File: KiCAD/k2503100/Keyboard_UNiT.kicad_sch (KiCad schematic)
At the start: 71 parts, among them J1 Power, J2 PWM, J3 Analog, J4 PWM, J5 Analog, J6 Communication, J7 Digital, SW1 SW_SPDT, SW10 SW_SPDT, SW11 SW_SPDT, SW12 SW_SPDT, SW13 SW_SPDT, SW14 SW_SPDT, SW15 SW_SPDT, SW16 SW_SPDT, SW17 SW_SPDT, SW18 SW_SPDT, SW19 SW_SPDT, SW2 SW_SPDT, SW20 SW_SPDT, SW21 SW_SPDT, SW22 SW_SPDT, SW23 SW_SPDT, SW24 SW_SPDT, SW25 SW_SPDT, SW26 SW_SPDT, SW27 SW_SPDT, SW28 SW_SPDT, SW29 SW_SPDT, SW3 SW_SPDT, SW30 SW_SPDT, SW31 SW_SPDT, SW32 SW_SPDT, SW33 SW_SPDT, SW34 SW_SPDT, SW35 SW_SPDT, SW36 SW_SPDT, SW37 SW_SPDT, SW38 SW_SPDT, SW39 SW_SPDT, SW4 SW_SPDT, SW40 SW_SPDT, SW41 SW_SPDT, SW42 SW_SPDT, SW43 SW_SPDT, SW44 SW_SPDT, SW45 SW_SPDT, SW46 SW_SPDT, SW47 SW_SPDT, SW48 SW_SPDT, SW49 SW_SPDT, SW5 SW_SPDT, SW50 SW_SPDT, SW51 SW_SPDT, SW52 SW_SPDT, SW53 SW_SPDT, SW54 SW_SPDT, SW55 SW_SPDT, SW56 SW_SPDT, SW57 SW_SPDT, SW58 SW_SPDT, SW59 SW_SPDT, SW6 SW_SPDT, SW60 SW_SPDT, SW61 SW_SPDT, SW62 SW_SPDT, SW63 SW_SPDT, SW64 SW_SPDT, SW7 SW_SPDT, SW8 SW_SPDT, SW9 SW_SPDT

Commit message: 途中 Relay Unit
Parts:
- added D1, D10, D11, D12, D13, D14, D15, D16, D17, D18, D19, D2, D20, D21, D22, D23, D24, D25, D26, D27, D28, D29, D3, D30, D31, D32, D33, D34, D35, D36, D37, D38, D39, D4, D40, D41, D42, D43, D44, D45, D46, D47, D48, D49, D5, D50, D51, D52, D53, D54, D55, D56, D57, D58, D59, D6, D60, D61, D62, D63, D64, D7, D8, D9: 1N4148, Diode_THT:D_DO-35_SOD27_P7.62mm_Horizontal, symbol Diode:1N4148
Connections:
- net A0 is gone; now on net 54: J3.1 (Pin_1)
- net A1 is gone; now on net 55: J3.2 (Pin_2)
- net A10 is gone; now on net 64: J5.3 (Pin_3)
- net A11 is gone; now on net 65: J5.4 (Pin_4)
- net A12 is gone; now on net 66: J5.5 (Pin_5)
- net A13 is gone; now on net 67: J5.6 (Pin_6)
- net A14 is gone; now on net 68: J5.7 (Pin_7)
- net A15 is gone; now on net 69: J5.8 (Pin_8)
- net A2 is gone; now on net 56: J3.3 (Pin_3)
- net A3 is gone; now on net 57: J3.4 (Pin_4)
- net A4 is gone; now on net 58: J3.5 (Pin_5)
- net A5 is gone; now on net 59: J3.6 (Pin_6)
- net A6 is gone; now on net 60: J3.7 (Pin_7)
- net A7 is gone; now on net 61: J3.8 (Pin_8)
- net A8 is gone; now on net 62: J5.1 (Pin_1)
- net A9 is gone; now on net 63: J5.2 (Pin_2)
- net *10: now also D7.1 (K)
- net *11: now also D8.1 (K)
- net *12: now also D9.1 (K)
- net *13: now also D10.1 (K)
- net *2: now also D1.2 (A), D10.2 (A), D11.2 (A), D12.2 (A), D13.2 (A), D14.2 (A), D15.2 (A), D16.2 (A), D17.2 (A), D18.2 (A), D19.2 (A), D2.2 (A), D20.2 (A), D21.2 (A), D22.2 (A), D23.2 (A), D24.2 (A), D25.2 (A), D26.2 (A), D27.2 (A), D28.2 (A), D29.2 (A), D3.2 (A), D30.2 (A), D31.2 (A), D32.2 (A), D4.2 (A), D5.2 (A), D6.2 (A), D7.2 (A), D8.2 (A), D9.2 (A)
- net *3: now also D33.2 (A), D34.2 (A), D35.2 (A), D36.2 (A), D37.2 (A), D38.2 (A), D39.2 (A), D40.2 (A), D41.2 (A), D42.2 (A), D43.2 (A), D44.2 (A), D45.2 (A), D46.2 (A), D47.2 (A), D48.2 (A), D49.2 (A), D50.2 (A), D51.2 (A), D52.2 (A), D53.2 (A), D54.2 (A), D55.2 (A), D56.2 (A), D57.2 (A), D58.2 (A), D59.2 (A), D60.2 (A), D61.2 (A), D62.2 (A), D63.2 (A), D64.2 (A)
- net *4: now also D1.1 (K)
- net *5: now also D2.1 (K)
- net *6: now also D3.1 (K)
- net *7: now also D4.1 (K)
- net *8: now also D5.1 (K)
- net *9: now also D6.1 (K)
- net 22: now also SW17.2 (B), D17.1 (K)
- net 23: now also SW18.2 (B), D18.1 (K)
- net 24: now also SW19.2 (B), D19.1 (K)
- net 25: now also SW20.2 (B), D20.1 (K)
- net 26: now also SW21.2 (B), D21.1 (K)
- net 27: now also SW22.2 (B), D22.1 (K)
- net 28: now also SW23.2 (B), D23.1 (K)
- net 29: now also SW24.2 (B), D24.1 (K)
- net 30: now also SW25.2 (B), D25.1 (K)
- net 31: now also SW26.2 (B), D26.1 (K)
- net 32: now also SW27.2 (B), D27.1 (K)
- net 33: now also SW28.2 (B), D28.1 (K)
- net 34: now also SW29.2 (B), D29.1 (K)
- net 35: now also SW30.2 (B), D30.1 (K)
- net 36: now also SW31.2 (B), D31.1 (K)
- net 37: now also SW32.2 (B), D32.1 (K)
- net 38: now also SW33.2 (B), D33.1 (K)
- net 39: now also SW34.2 (B), D34.1 (K)
- net 40: now also SW35.2 (B), D35.1 (K)
- net 41: now also SW36.2 (B), D36.1 (K)
- net 42: now also SW37.2 (B), D37.1 (K)
- net 43: now also SW38.2 (B), D38.1 (K)
- net 47: now also SW42.2 (B), D42.1 (K)
- net 48: now also SW43.2 (B), D43.1 (K)
- net 49: now also SW44.2 (B), D44.1 (K)
- net 50: now also SW45.2 (B), D45.1 (K)
- net 51: now also SW46.2 (B), D46.1 (K)
- net 53: now also SW48.2 (B), D48.1 (K)
- net 65: now reaches SW60.2 (B)
- net 65: now also D60.1 (K)
- net 55: now reaches SW50.2 (B)
- net 55: now also D50.1 (K)
- net 57: now reaches SW52.2 (B)
- net 57: now also D52.1 (K)
- net 58: now reaches SW53.2 (B)
- net 58: now also D53.1 (K)
- net 54: now reaches SW49.2 (B)
- net 54: now also D49.1 (K)
- net 60: now reaches SW55.2 (B)
- net 60: now also D55.1 (K)
- net 52: now reaches SW47.2 (B)
- net 52: now also D47.1 (K)
- net 66: now reaches SW61.2 (B)
- net 66: now also D61.1 (K)
- net 44: now reaches SW39.2 (B)
- net 44: now also D39.1 (K)
- net 45: now reaches SW40.2 (B)
- net 45: now also D40.1 (K)
- net 62: now reaches SW57.2 (B)
- net 62: now also D57.1 (K)
- net 59: now reaches SW54.2 (B)
- net 59: now also D54.1 (K)
- net 64: now reaches SW59.2 (B)
- net 64: now also D59.1 (K)
- net 56: now reaches SW51.2 (B)
- net 56: now also D51.1 (K)
- net 68: now reaches SW63.2 (B)
- net 68: now also D63.1 (K)
- net 46: now reaches SW41.2 (B)
- net 46: now also D41.1 (K)
- net 63: now reaches SW58.2 (B)
- net 63: now also D58.1 (K)
- net 69: now reaches SW64.2 (B)
- net 69: now also D64.1 (K)
- net 67: now reaches SW62.2 (B)
- net 67: now also D62.1 (K)
- net 61: now reaches SW56.2 (B)
- net 61: now also D56.1 (K)
- no-connect marks 67 -> 69
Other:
- company: (none) -> HOLLY&Co.,Ltd.
- title: (none) -> Keyboard Unit

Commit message: KiCAD 8
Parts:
- renumbered J3 to J2, J5 to J3, J7 to J4, J2 to J5, J4 to J6, J6 to J7
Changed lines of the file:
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@@
     (instances
       (project "k2503100"
-        (path "/e63e39d7-6ac0-4ffd-8aa3-1841a4541b55"
-          (reference "J1") (unit 1)
-        )
         (path "/e63e39d7-6ac0-4ffd-8aa3-1841a4541b55/1b167d0b-8840-4de9-be2c-713538496dc4"
           (reference "J1") (unit 1)
@@
     (instances
       (project "k2503100"
-        (path "/e63e39d7-6ac0-4ffd-8aa3-1841a4541b55"
-          (reference "#PWR01") (unit 1)
-        )
         (path "/e63e39d7-6ac0-4ffd-8aa3-1841a4541b55/1b167d0b-8840-4de9-be2c-713538496dc4"
           (reference "#PWR01") (unit 1)
@@
   (symbol (lib_id "power:GND") (at 20.32 189.23 0) (unit 1)
     (in_bom yes) (on_board yes) (dnp no)
-    (property "Reference" "#PWR07" (at 20.32 195.58 0)
+    (property "Reference" "#PWR027" (at 20.32 195.58 0)
       (effects (font (size 1.27 1.27)) hide)
     )
@@
     (instances
       (project "k2503100"
-        (path "/e63e39d7-6ac0-4ffd-8aa3-1841a4541b55"
-          (reference "#PWR07") (unit 1)
-        )
         (path "/e63e39d7-6ac0-4ffd-8aa3-1841a4541b55/1b167d0b-8840-4de9-be2c-713538496dc4"
           (reference "#PWR027") (unit 1)
@@
   (symbol (lib_id "Connector_Generic:Conn_01x08") (at 203.2 97.79 0) (mirror y) (unit 1)
     (in_bom yes) (on_board yes) (dnp no)
-    (property "Reference" "J6" (at 203.2 87.63 0)
+    (property "Reference" "J7" (at 203.2 87.63 0)
       (effects (font (size 1.27 1.27)))
     )
@@
     (instances
       (project "k2503100"
-        (path "/e63e39d7-6ac0-4ffd-8aa3-1841a4541b55"
-          (reference "J6") (unit 1)
-        )
         (path "/e63e39d7-6ac0-4ffd-8aa3-1841a4541b55/1b167d0b-8840-4de9-be2c-713538496dc4"
           (reference "J7") (unit 1)
@@
   (symbol (lib_id "power:GND") (at 80.01 189.23 0) (unit 1)
     (in_bom yes) (on_board yes) (dnp no)
-    (property "Reference" "#PWR07" (at 80.01 195.58 0)
+    (property "Reference" "#PWR025" (at 80.01 195.58 0)
       (effects (font (size 1.27 1.27)) hide)
     )
@@
     (instances
       (project "k2503100"
-        (path "/e63e39d7-6ac0-4ffd-8aa3-1841a4541b55"
-          (reference "#PWR07") (unit 1)
-        )
         (path "/e63e39d7-6ac0-4ffd-8aa3-1841a4541b55/1b167d0b-8840-4de9-be2c-713538496dc4"
           (reference "#PWR025") (unit 1)
@@
     (instances
       (project "k2503100"
-        (path "/e63e39d7-6ac0-4ffd-8aa3-1841a4541b55"
-          (reference "#PWR06") (unit 1)
-        )
         (path "/e63e39d7-6ac0-4ffd-8aa3-1841a4541b55/1b167d0b-8840-4de9-be2c-713538496dc4"
           (reference "#PWR06") (unit 1)
@@
   (symbol (lib_id "Connector_Generic:Conn_01x08") (at 185.42 72.39 0) (unit 1)
     (in_bom yes) (on_board yes) (dnp no)
-    (property "Reference" "J3" (at 185.42 62.23 0)
+    (property "Reference" "J2" (at 185.42 62.23 0)
       (effects (font (size 1.27 1.27)))
     )
@@
     (instances
       (project "k2503100"
-        (path "/e63e39d7-6ac0-4ffd-8aa3-1841a4541b55"
-          (reference "J3") (unit 1)
-        )
         (path "/e63e39d7-6ac0-4ffd-8aa3-1841a4541b55/1b167d0b-8840-4de9-be2c-713538496dc4"
           (reference "J2") (unit 1)
@@
   (symbol (lib_id "power:GND") (at 109.22 189.23 0) (unit 1)
     (in_bom yes) (on_board yes) (dnp no)
-    (property "Reference" "#PWR07" (at 109.22 195.58 0)
+    (property "Reference" "#PWR024" (at 109.22 195.58 0)
       (effects (font (size 1.27 1.27)) hide)
     )
@@
     (instances
       (project "k2503100"
-        (path "/e63e39d7-6ac0-4ffd-8aa3-1841a4541b55"
-          (reference "#PWR07") (unit 1)
-        )
         (path "/e63e39d7-6ac0-4ffd-8aa3-1841a4541b55/1b167d0b-8840-4de9-be2c-713538496dc4"
           (reference "#PWR024") (unit 1)
@@
   (symbol (lib_id "Connector_Generic:Conn_01x08") (at 203.2 72.39 0) (mirror y) (unit 1)
     (in_bom yes) (on_board yes) (dnp no)
-    (property "Reference" "J4" (at 203.2 62.23 0)
+    (property "Reference" "J6" (at 203.2 62.23 0)
       (effects (font (size 1.27 1.27)))
     )
@@
     (instances
       (project "k2503100"
-        (path "/e63e39d7-6ac0-4ffd-8aa3-1841a4541b55"
-          (reference "J4") (unit 1)
-        )
         (path "/e63e39d7-6ac0-4ffd-8aa3-1841a4541b55/1b167d0b-8840-4de9-be2c-713538496dc4"
           (reference "J6") (unit 1)
@@
   (symbol (lib_id "Connector_Generic:Conn_02x18_Odd_Even") (at 195.58 138.43 90) (mirror x) (unit 1)
     (in_bom yes) (on_board yes) (dnp no)
-    (property "Reference" "J7" (at 173.2279 139.8206 90)
+    (property "Reference" "J4" (at 173.2279 139.8206 90)
       (effects (font (size 1.27 1.27)) (justify left))
     )
@@
     (instances
       (project "k2503100"
-        (path "/e63e39d7-6ac0-4ffd-8aa3-1841a4541b55"
-          (reference "J7") (unit 1)
-        )
         (path "/e63e39d7-6ac0-4ffd-8aa3-1841a4541b55/1b167d0b-8840-4de9-be2c-713538496dc4"
           (reference "J4") (unit 1)
@@
   (symbol (lib_id "power:GND") (at 270.51 27.94 0) (unit 1)
     (in_bom yes) (on_board yes) (dnp no)
-    (property "Reference" "#PWR05" (at 270.51 34.29 0)
+    (property "Reference" "#PWR023" (at 270.51 34.29 0)
       (effects (font (size 1.27 1.27)) hide)
     )
@@
     (instances
       (project "k2503100"
-        (path "/e63e39d7-6ac0-4ffd-8aa3-1841a4541b55"
-          (reference "#PWR05") (unit 1)
-        )
         (path "/e63e39d7-6ac0-4ffd-8aa3-1841a4541b55/1b167d0b-8840-4de9-be2c-713538496dc4"
           (reference "#PWR023") (unit 1)
@@
     (instances
       (project "k2503100"
-        (path "/e63e39d7-6ac0-4ffd-8aa3-1841a4541b55"
-          (reference "#PWR03") (unit 1)
-        )
         (path "/e63e39d7-6ac0-4ffd-8aa3-1841a4541b55/1b167d0b-8840-4de9-be2c-713538496dc4"
           (reference "#PWR03") (unit 1)
@@
   (symbol (lib_id "power:GND") (at 49.53 189.23 0) (unit 1)
     (in_bom yes) (on_board yes) (dnp no)
-    (property "Reference" "#PWR07" (at 49.53 195.58 0)
+    (property "Reference" "#PWR026" (at 49.53 195.58 0)
       (effects (font (size 1.27 1.27)) hide)
     )
@@
     (instances
       (project "k2503100"
-        (path "/e63e39d7-6ac0-4ffd-8aa3-1841a4541b55"
-          (reference "#PWR07") (unit 1)
-        )
         (path "/e63e39d7-6ac0-4ffd-8aa3-1841a4541b55/1b167d0b-8840-4de9-be2c-713538496dc4"
           (reference "#PWR026") (unit 1)
@@
   (symbol (lib_id "power:GND") (at 210.82 57.15 0) (unit 1)
     (in_bom yes) (on_board yes) (dnp no)
-    (property "Reference" "#PWR05" (at 210.82 63.5 0)
+    (property "Reference" "#PWR07" (at 210.82 63.5 0)
       (effects (font (size 1.27 1.27)) hide)
     )
@@
     (instances
       (project "k2503100"
-        (path "/e63e39d7-6ac0-4ffd-8aa3-1841a4541b55"
-          (reference "#PWR05") (unit 1)
-        )
         (path "/e63e39d7-6ac0-4ffd-8aa3-1841a4541b55/1b167d0b-8840-4de9-be2c-713538496dc4"
           (reference "#PWR07") (unit 1)
@@
   (symbol (lib_id "Connector_Generic:Conn_01x10") (at 203.2 41.91 0) (mirror y) (unit 1)
     (in_bom yes) (on_board yes) (dnp no)
-    (property "Reference" "J2" (at 203.2 29.21 0)
+    (property "Reference" "J5" (at 203.2 29.21 0)
       (effects (font (size 1.27 1.27)))
     )
@@
     (instances
       (project "k2503100"
-        (path "/e63e39d7-6ac0-4ffd-8aa3-1841a4541b55"
-          (reference "J2") (unit 1)
-        )
         (path "/e63e39d7-6ac0-4ffd-8aa3-1841a4541b55/1b167d0b-8840-4de9-be2c-713538496dc4"
           (reference "J5") (unit 1)
@@
   (symbol (lib_id "power:+5V") (at 273.05 17.78 0) (unit 1)
     (in_bom yes) (on_board yes) (dnp no)
-    (property "Reference" "#PWR02" (at 273.05 21.59 0)
+    (property "Reference" "#PWR022" (at 273.05 21.59 0)
       (effects (font (size 1.27 1.27)) hide)
     )
@@
     (instances
       (project "k2503100"
-        (path "/e63e39d7-6ac0-4ffd-8aa3-1841a4541b55"
-          (reference "#PWR02") (unit 1)
-        )
         (path "/e63e39d7-6ac0-4ffd-8aa3-1841a4541b55/1b167d0b-8840-4de9-be2c-713538496dc4"
           (reference "#PWR022") (unit 1)
@@
   (symbol (lib_id "Connector_Generic:Conn_01x08") (at 185.42 97.79 0) (unit 1)
     (in_bom yes) (on_board yes) (dnp no)
-    (property "Reference" "J5" (at 185.42 87.63 0)
+    (property "Reference" "J3" (at 185.42 87.63 0)
       (effects (font (size 1.27 1.27)))
     )
@@
     (instances
       (project "k2503100"
-        (path "/e63e39d7-6ac0-4ffd-8aa3-1841a4541b55"
-          (reference "J5") (unit 1)
-        )
         (path "/e63e39d7-6ac0-4ffd-8aa3-1841a4541b55/1b167d0b-8840-4de9-be2c-713538496dc4"
           (reference "J3") (unit 1)
@@
     (instances
       (project "k2503100"
-        (path "/e63e39d7-6ac0-4ffd-8aa3-1841a4541b55"
-          (reference "#PWR04") (unit 1)
-        )
         (path "/e63e39d7-6ac0-4ffd-8aa3-1841a4541b55/1b167d0b-8840-4de9-be2c-713538496dc4"
           (reference "#PWR04") (unit 1)
@@
     (instances
       (project "k2503100"
-        (path "/e63e39d7-6ac0-4ffd-8aa3-1841a4541b55"
-          (reference "#PWR02") (unit 1)
-        )
         (path "/e63e39d7-6ac0-4ffd-8aa3-1841a4541b55/1b167d0b-8840-4de9-be2c-713538496dc4"
           (reference "#PWR02") (unit 1)
@@
   (symbol (lib_id "power:GND") (at 170.18 153.67 0) (unit 1)
     (in_bom yes) (on_board yes) (dnp no)
-    (property "Reference" "#PWR07" (at 170.18 160.02 0)
+    (property "Reference" "#PWR05" (at 170.18 160.02 0)
       (effects (font (size 1.27 1.27)) hide)
     )
@@
     (instances
       (project "k2503100"
-        (path "/e63e39d7-6ac0-4ffd-8aa3-1841a4541b55"
-          (reference "#PWR07") (unit 1)
-        )
         (path "/e63e39d7-6ac0-4ffd-8aa3-1841a4541b55/1b167d0b-8840-4de9-be2c-713538496dc4"
           (reference "#PWR05") (unit 1)

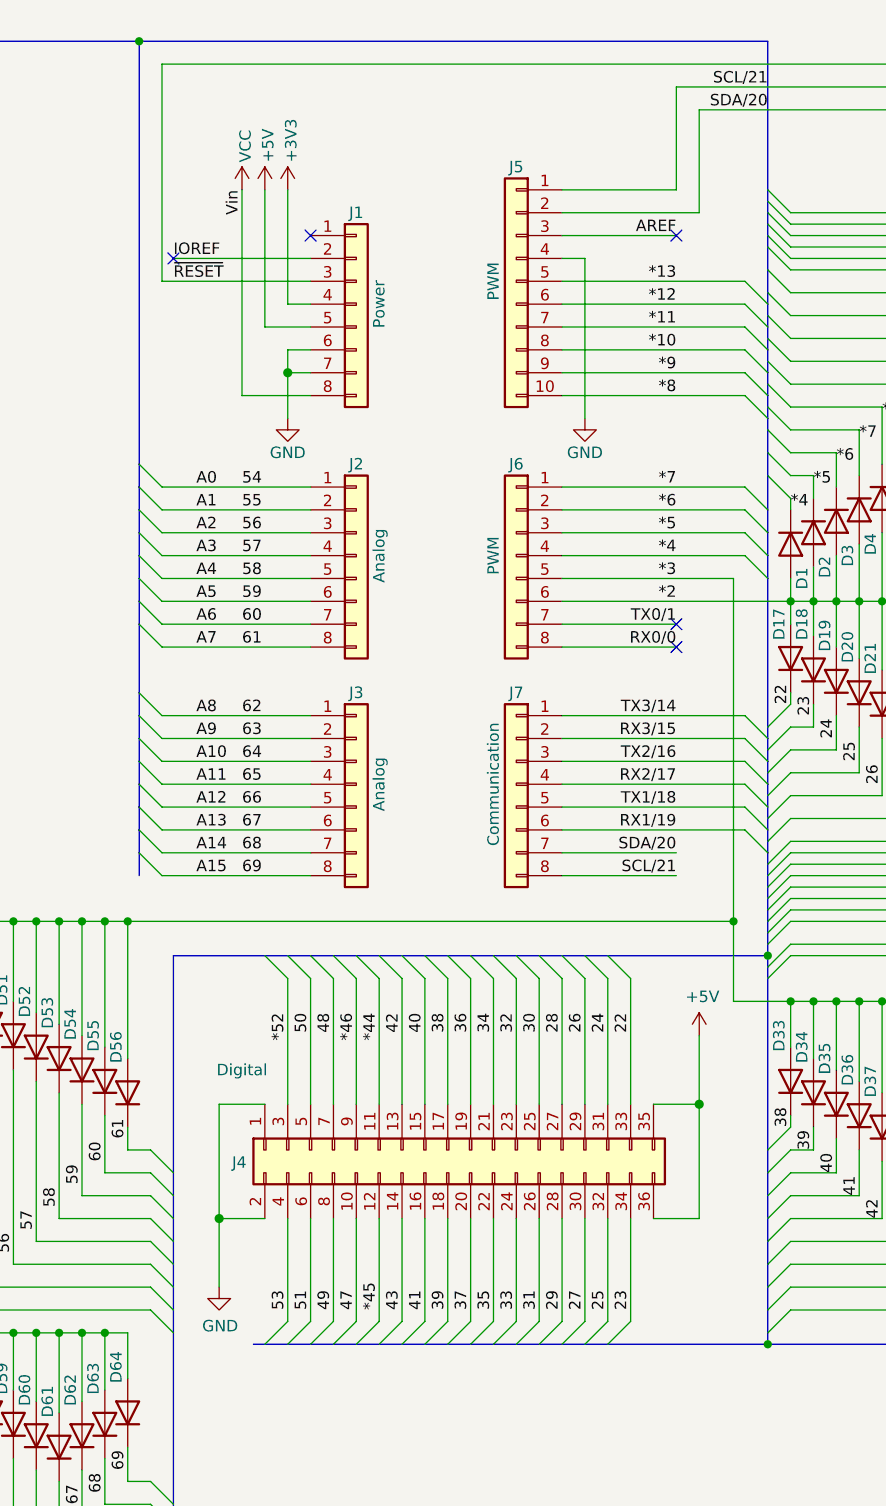
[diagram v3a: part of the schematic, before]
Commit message: MP86A1のパーツ作成
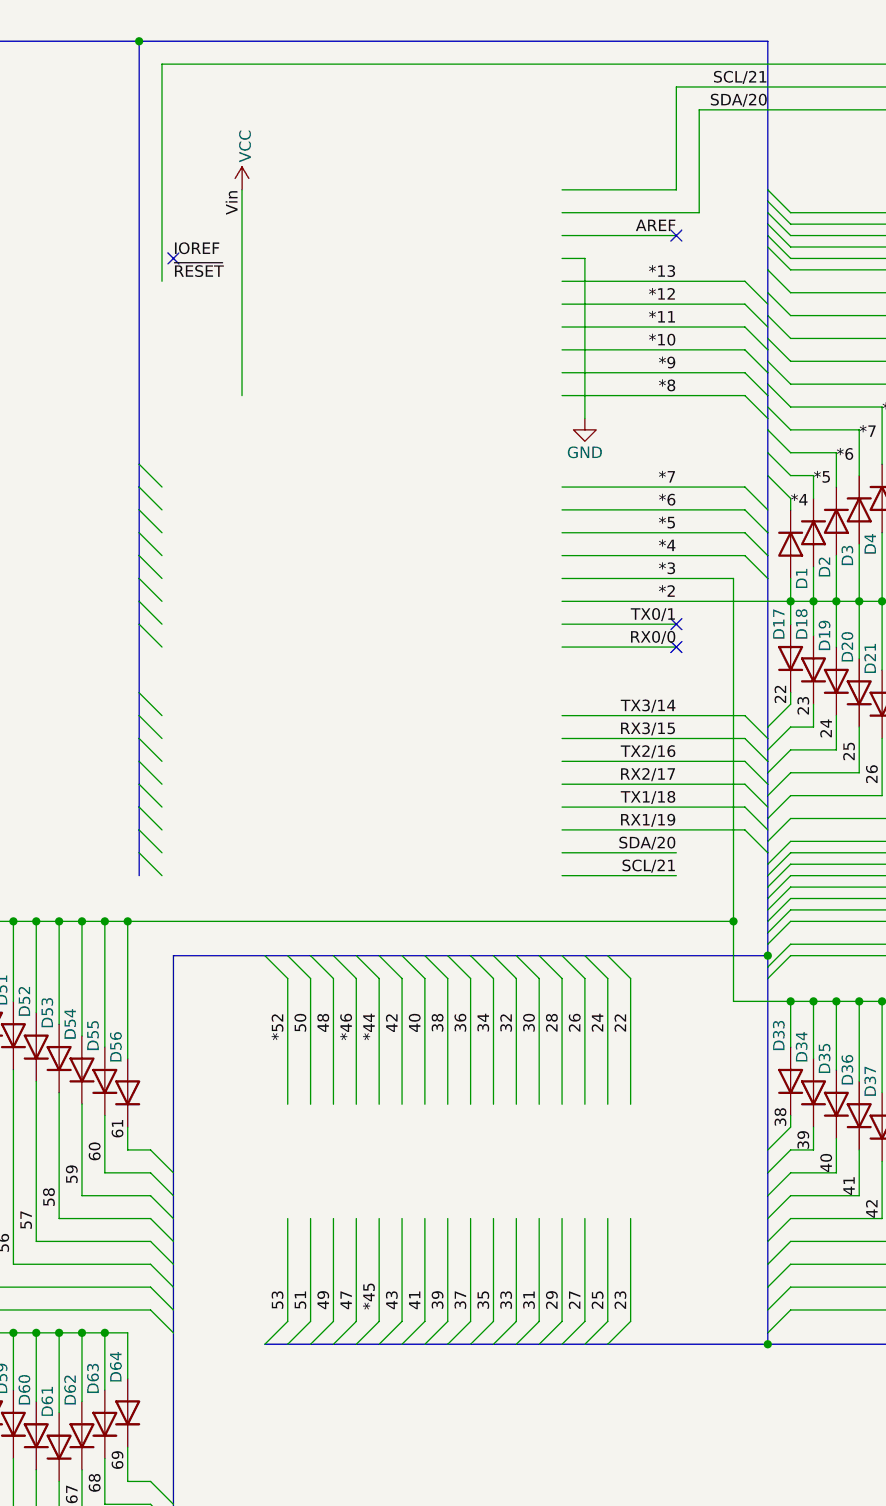
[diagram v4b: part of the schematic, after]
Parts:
- removed J1: Power, Connector_PinSocket_2.54mm:PinSocket_1x08_P2.54mm_Vertical, symbol Connector_Generic:Conn_01x08
- removed J2, J3: Analog, Connector_PinSocket_2.54mm:PinSocket_1x08_P2.54mm_Vertical, symbol Connector_Generic:Conn_01x08
- removed J4: Digital, Connector_PinSocket_2.54mm:PinSocket_2x18_P2.54mm_Vertical, symbol Connector_Generic:Conn_02x18_Odd_Even
- removed J5: PWM, Connector_PinSocket_2.54mm:PinSocket_1x10_P2.54mm_Vertical, symbol Connector_Generic:Conn_01x10
- removed J6: PWM, Connector_PinSocket_2.54mm:PinSocket_1x08_P2.54mm_Vertical, symbol Connector_Generic:Conn_01x08
- removed J7: Communication, Connector_PinSocket_2.54mm:PinSocket_1x08_P2.54mm_Vertical, symbol Connector_Generic:Conn_01x08
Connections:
- no-connect marks 69 -> 68
